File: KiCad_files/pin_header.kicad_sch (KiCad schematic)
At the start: 1 part, among them J1 Conn_01x08_Socket

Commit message: pwr_flags
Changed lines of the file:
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@@
 	(generator_version "9.0")
 	(paper "A4")
+	(junction
+		(at 186.69 110.49)
+		(diameter 0)
+		(color 0 0 0 0)
+	)
 	(wire
 		(pts
@@
 	(wire
 		(pts
+			(xy 186.69 110.49) (xy 190.5 110.49)
+		)
+		(stroke
+			(width 0)
+			(type default)
+		)
+	)
+	(wire
+		(pts
 			(xy 161.29 105.41) (xy 165.1 105.41)
 		)
@@
 	(wire
 		(pts
-			(xy 161.29 110.49) (xy 165.1 110.49)
+			(xy 161.29 110.49) (xy 186.69 110.49)
 		)
 		(stroke
@@
 	(hierarchical_label "BAT"
 		(shape output)
-		(at 165.1 110.49 0)
+		(at 190.5 110.49 0)
 		(effects
 			(font
@@
 		)
 	)
+	(symbol
+		(lib_id "power:PWR_FLAG")
+		(at 186.69 110.49 0)
+		(unit 1)
+		(exclude_from_sim no)
+		(in_bom yes)
+		(on_board yes)
+		(dnp no)
+		(fields_autoplaced yes)
+		(property "Reference" "#FLG02"
+			(at 186.69 108.585 0)
+			(effects
+				(font
+					(size 1.27 1.27)
+				)
+				(hide yes)
+			)
+		)
+		(property "Value" "PWR_FLAG"
+			(at 186.69 105.41 0)
+			(effects
+				(font
+					(size 1.27 1.27)
+				)
+			)
+		)
+		(property "Footprint" ""
+			(at 186.69 110.49 0)
+			(effects
+				(font
+					(size 1.27 1.27)
+				)
+				(hide yes)
+			)
+		)
+		(property "Datasheet" "~"
+			(at 186.69 110.49 0)
+			(effects
+				(font
+					(size 1.27 1.27)
+				)
+				(hide yes)
+			)
+		)
+		(property "Description" "Special symbol for telling ERC where power comes from"
+			(at 186.69 110.49 0)
+			(effects
+				(font
+					(size 1.27 1.27)
+				)
+				(hide yes)
+			)
+		)
+		(pin "1"
+		)
+		(instances
+			(project ""
+				(path "/186d5500-054c-4b47-a89c-85f6ce2abe33/e57caa54-6ff3-4f9e-a4cf-b739534fbed5"
+					(reference "#FLG02")
+					(unit 1)
+				)
+			)
+		)
+	)

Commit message: JTAG
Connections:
- net BAT: now also J1.3 (Pin_3); no longer J1.4 (Pin_4)
- new net JTAG_SEL: J1.4 (Pin_4)
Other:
- note added: "Pull JTAG_SEL down during boot to enable auxiliary JTAG interface"
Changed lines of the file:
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@@
 	(generator_version "9.0")
 	(paper "A4")
+	(text "Pull JTAG_SEL down during boot to enable auxiliary JTAG interface"
+		(exclude_from_sim no)
+		(at 176.53 88.138 0)
+		(effects
+			(font
+				(size 1.27 1.27)
+			)
+		)
+	)
 	(junction
-		(at 186.69 110.49)
+		(at 186.69 113.03)
 		(diameter 0)
 		(color 0 0 0 0)
@@
 	(wire
 		(pts
-			(xy 186.69 110.49) (xy 190.5 110.49)
+			(xy 186.69 113.03) (xy 190.5 113.03)
 		)
 		(stroke
@@
 	(wire
 		(pts
+			(xy 190.5 121.92) (xy 190.5 115.57)
+		)
+		(stroke
+			(width 0)
+			(type default)
+		)
+	)
+	(wire
+		(pts
+			(xy 161.29 113.03) (xy 186.69 113.03)
+		)
+		(stroke
+			(width 0)
+			(type default)
+		)
+	)
+	(wire
+		(pts
 			(xy 161.29 102.87) (xy 165.1 102.87)
 		)
@@
 	(wire
 		(pts
-			(xy 190.5 121.92) (xy 190.5 115.57)
-		)
-		(stroke
-			(width 0)
-			(type default)
-		)
-	)
-	(wire
-		(pts
-			(xy 161.29 110.49) (xy 186.69 110.49)
-		)
-		(stroke
-			(width 0)
-			(type default)
-		)
-	)
-	(wire
-		(pts
 			(xy 177.8 118.11) (xy 161.29 118.11)
 		)
@@
 		(pts
 			(xy 177.8 121.92) (xy 177.8 118.11)
+		)
+		(stroke
+			(width 0)
+			(type default)
+		)
+	)
+	(wire
+		(pts
+			(xy 161.29 110.49) (xy 165.1 110.49)
 		)
 		(stroke
@@
 	(hierarchical_label "BAT"
 		(shape output)
-		(at 190.5 110.49 0)
+		(at 190.5 113.03 0)
 		(effects
 			(font
@@
 		(shape input)
 		(at 165.1 102.87 0)
+		(effects
+			(font
+				(size 1.27 1.27)
+			)
+			(justify left)
+		)
+	)
+	(hierarchical_label "JTAG_SEL"
+		(shape output)
+		(at 165.1 110.49 0)
 		(effects
 			(font
@@
 	(symbol
 		(lib_id "power:PWR_FLAG")
-		(at 186.69 110.49 0)
+		(at 186.69 113.03 0)
 		(unit 1)
 		(exclude_from_sim no)
@@
 		(fields_autoplaced yes)
 		(property "Reference" "#FLG02"
-			(at 186.69 108.585 0)
+			(at 186.69 111.125 0)
 			(effects
 				(font
@@
 		)
 		(property "Value" "PWR_FLAG"
-			(at 186.69 105.41 0)
+			(at 186.69 107.95 0)
 			(effects
 				(font
@@
 		)
 		(property "Footprint" ""
-			(at 186.69 110.49 0)
+			(at 186.69 113.03 0)
 			(effects
 				(font
@@
 		)
 		(property "Datasheet" "~"
-			(at 186.69 110.49 0)
+			(at 186.69 113.03 0)
 			(effects
 				(font
@@
 		)
 		(property "Description" "Special symbol for telling ERC where power comes from"
-			(at 186.69 110.49 0)
-			(effects
-				(font
+			(at 186.69 113.03 0)
+			(effects
+				(font

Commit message: ERC hiljennetty
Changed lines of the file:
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@@
 	(wire
 		(pts
-			(xy 190.5 115.57) (xy 161.29 115.57)
+			(xy 161.29 115.57) (xy 203.2 115.57)
 		)
 		(stroke
@@
 	(wire
 		(pts
-			(xy 190.5 121.92) (xy 190.5 115.57)
-		)
-		(stroke
-			(width 0)
-			(type default)
-		)
-	)
-	(wire
-		(pts
 			(xy 161.29 113.03) (xy 186.69 113.03)
 		)
@@
 		(pts
 			(xy 161.29 107.95) (xy 165.1 107.95)
+		)
+		(stroke
+			(width 0)
+			(type default)
+		)
+	)
+	(wire
+		(pts
+			(xy 203.2 115.57) (xy 203.2 113.03)
 		)
 		(stroke
@@
 			)
 			(justify left)
+		)
+	)
+	(symbol
+		(lib_id "power:+3.3V")
+		(at 203.2 113.03 0)
+		(unit 1)
+		(exclude_from_sim no)
+		(in_bom yes)
+		(on_board yes)
+		(dnp no)
+		(fields_autoplaced yes)
+		(property "Reference" "#PWR03"
+			(at 203.2 116.84 0)
+			(effects
+				(font
+					(size 1.27 1.27)
+				)
+				(hide yes)
+			)
+		)
+		(property "Value" "+3.3V"
+			(at 203.2 107.95 0)
+			(effects
+				(font
+					(size 1.27 1.27)
+				)
+			)
+		)
+		(property "Footprint" ""
+			(at 203.2 113.03 0)
+			(effects
+				(font
+					(size 1.27 1.27)
+				)
+				(hide yes)
+			)
+		)
+		(property "Datasheet" ""
+			(at 203.2 113.03 0)
+			(effects
+				(font
+					(size 1.27 1.27)
+				)
+				(hide yes)
+			)
+		)
+		(property "Description" "Power symbol creates a global label with name \"+3.3V\""
+			(at 203.2 113.03 0)
+			(effects
+				(font
+					(size 1.27 1.27)
+				)
+				(hide yes)
+			)
+		)
+		(pin "1"
+		)
+		(instances
+			(project ""
+				(path "/186d5500-054c-4b47-a89c-85f6ce2abe33/e57caa54-6ff3-4f9e-a4cf-b739534fbed5"
+					(reference "#PWR03")
+					(unit 1)
+				)
+			)
 		)
 	)
@@
 					(unit 1)
 				)
-			)
-		)
-	)
-	(symbol
-		(lib_id "power:+3.3V")
-		(at 190.5 121.92 180)
-		(unit 1)
-		(exclude_from_sim no)
-		(in_bom yes)
-		(on_board yes)
-		(dnp no)
-		(fields_autoplaced yes)
-		(property "Reference" "#PWR03"
-			(at 190.5 118.11 0)
-			(effects
-				(font
-					(size 1.27 1.27)
-				)
-				(hide yes)
-			)
-		)
-		(property "Value" "+3.3V"
-			(at 190.5 127 0)
-			(effects
-				(font
-					(size 1.27 1.27)
-				)
-			)
-		)
-		(property "Footprint" ""
-			(at 190.5 121.92 0)
-			(effects
-				(font
-					(size 1.27 1.27)
-				)
-				(hide yes)
-			)
-		)
-		(property "Datasheet" ""
-			(at 190.5 121.92 0)
-			(effects
-				(font
-					(size 1.27 1.27)
-				)
-				(hide yes)
-			)
-		)
-		(property "Description" "Power symbol creates a global label with name \"+3.3V\""
-			(at 190.5 121.92 0)
-			(effects
-				(font
-					(size 1.27 1.27)
-				)
-				(hide yes)
-			)
-		)
-		(pin "1"
-		)
-		(instances
-			(project ""
-				(path "/186d5500-054c-4b47-a89c-85f6ce2abe33/e57caa54-6ff3-4f9e-a4cf-b739534fbed5"
-					(reference "#PWR03")
-					(unit 1)
-				)

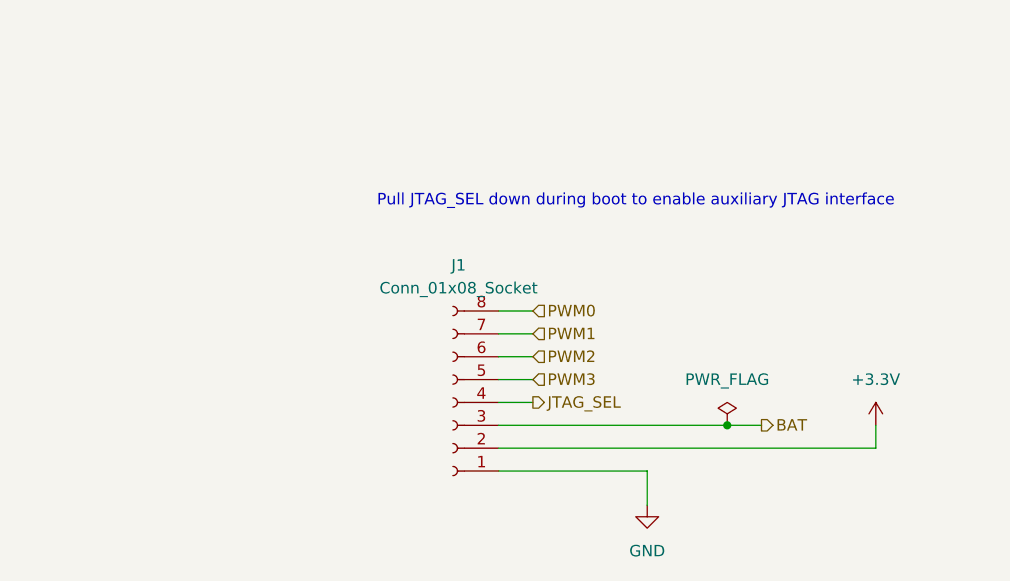
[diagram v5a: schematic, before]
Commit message: headerit mietitty, pinnijärjestystä muutettu mcussa
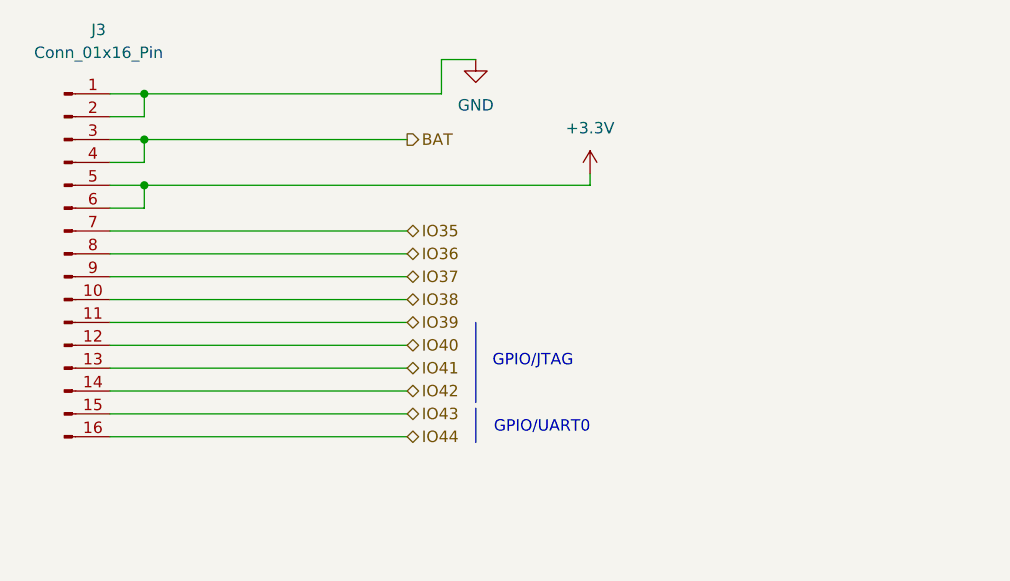
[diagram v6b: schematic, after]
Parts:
- removed J1: Conn_01x08_Socket, Connector_PinSocket_2.54mm:PinSocket_1x08_P2.54mm_Vertical, symbol Connector:Conn_01x08_Socket
- added J3: Conn_01x16_Pin, Connector_PinHeader_2.54mm:PinHeader_1x16_P2.54mm_Vertical, symbol Connector:Conn_01x16_Pin
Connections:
- net +3.3V: now also J3.5 (Pin_5), J3.6 (Pin_6)
- net BAT: now also J3.3 (Pin_3), J3.4 (Pin_4)
- net GND: now also J3.1 (Pin_1), J3.2 (Pin_2)
- new net IO35: J3.7 (Pin_7)
- new net IO36: J3.8 (Pin_8)
- new net IO37: J3.9 (Pin_9)
- new net IO38: J3.10 (Pin_10)
- new net IO39: J3.11 (Pin_11)
- new net IO40: J3.12 (Pin_12)
- new net IO41: J3.13 (Pin_13)
- new net IO42: J3.14 (Pin_14)
- new net IO43: J3.15 (Pin_15)
- new net IO44: J3.16 (Pin_16)
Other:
- note added: "GPIO/JTAG"
- note added: "GPIO/UART0"
- note removed: "Pull JTAG_SEL down during boot to enable auxiliary JTAG interface"

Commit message: wippistä
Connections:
- net +3.3V: now also J3.15 (Pin_15), J3.16 (Pin_16); no longer J3.5 (Pin_5), J3.6 (Pin_6)
- net BAT: now also J3.13 (Pin_13), J3.14 (Pin_14); no longer J3.3 (Pin_3), J3.4 (Pin_4)
- net GND: now also J3.11 (Pin_11), J3.12 (Pin_12); no longer J3.1 (Pin_1), J3.2 (Pin_2)
- net IO35: now also J3.1 (Pin_1); no longer J3.7 (Pin_7)
- net IO36: now also J3.2 (Pin_2); no longer J3.8 (Pin_8)
- net IO37: now also J3.3 (Pin_3); no longer J3.9 (Pin_9)
- net IO38: now also J3.4 (Pin_4); no longer J3.10 (Pin_10)
- net IO39: now also J3.5 (Pin_5); no longer J3.11 (Pin_11)
- net IO40: now also J3.6 (Pin_6); no longer J3.12 (Pin_12)
- net IO41: now also J3.7 (Pin_7); no longer J3.13 (Pin_13)
- net IO42: now also J3.8 (Pin_8); no longer J3.14 (Pin_14)
- net IO43: now also J3.9 (Pin_9); no longer J3.15 (Pin_15)
- net IO44: now also J3.10 (Pin_10); no longer J3.16 (Pin_16)
